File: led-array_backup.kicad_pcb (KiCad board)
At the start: 4 copper layers, 180.2 x 119.8 mm, 1226 parts, among them J1 Conn_01x04_Pin, J2 USB_B_Micro, Q1 Q_NMOS_GDS, Q2 Q_NMOS_GDS, Q3 Q_NMOS_GDS, Q4 Q_NMOS_GDS, Q5 Q_NMOS_GDS, Q6 Q_NMOS_GDS, Q7 Q_NMOS_GDS, Q8 Q_NMOS_GDS, U1 TPS54331DR, U10 74HC595, U11 74HC595, U12 74HC595, U13 74HC595, U14 74HC595, U15 74HC595, U16 74HC595, U17 74HC595, U18 74HC595, U2 STM32F103C8T6, U3 74HC595, U4 74HC595, U5 74HC595, U6 74HC595, U7 74HC595, U8 74HC595, U9 74HC595, Y1 16MHz

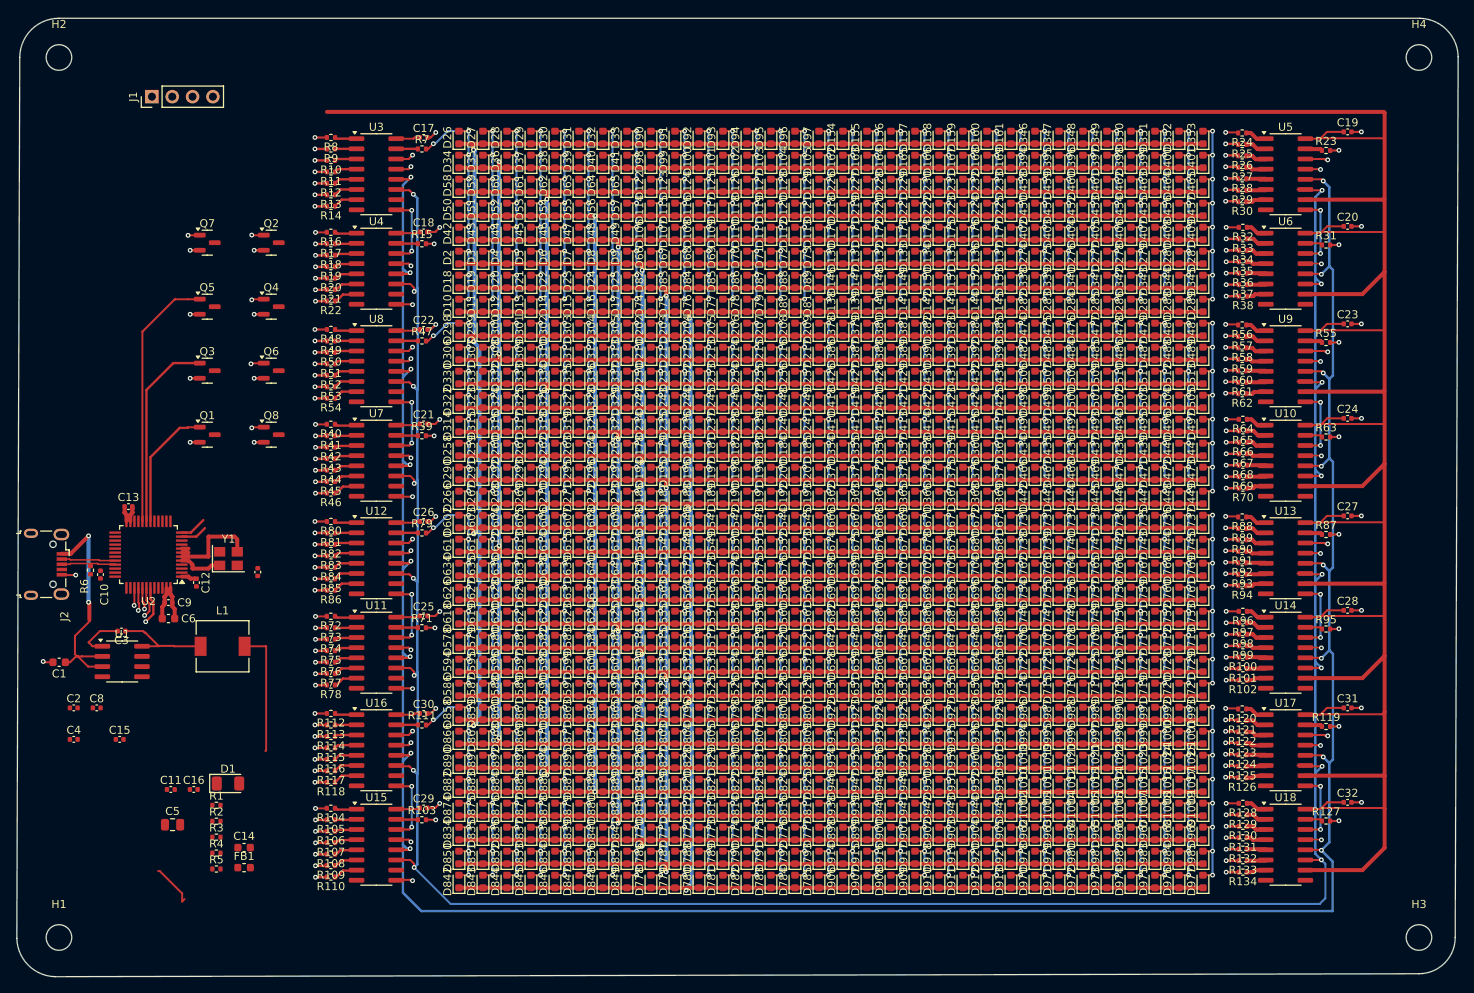
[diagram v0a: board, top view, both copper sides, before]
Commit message: Set up RCLK and SRCLK lines
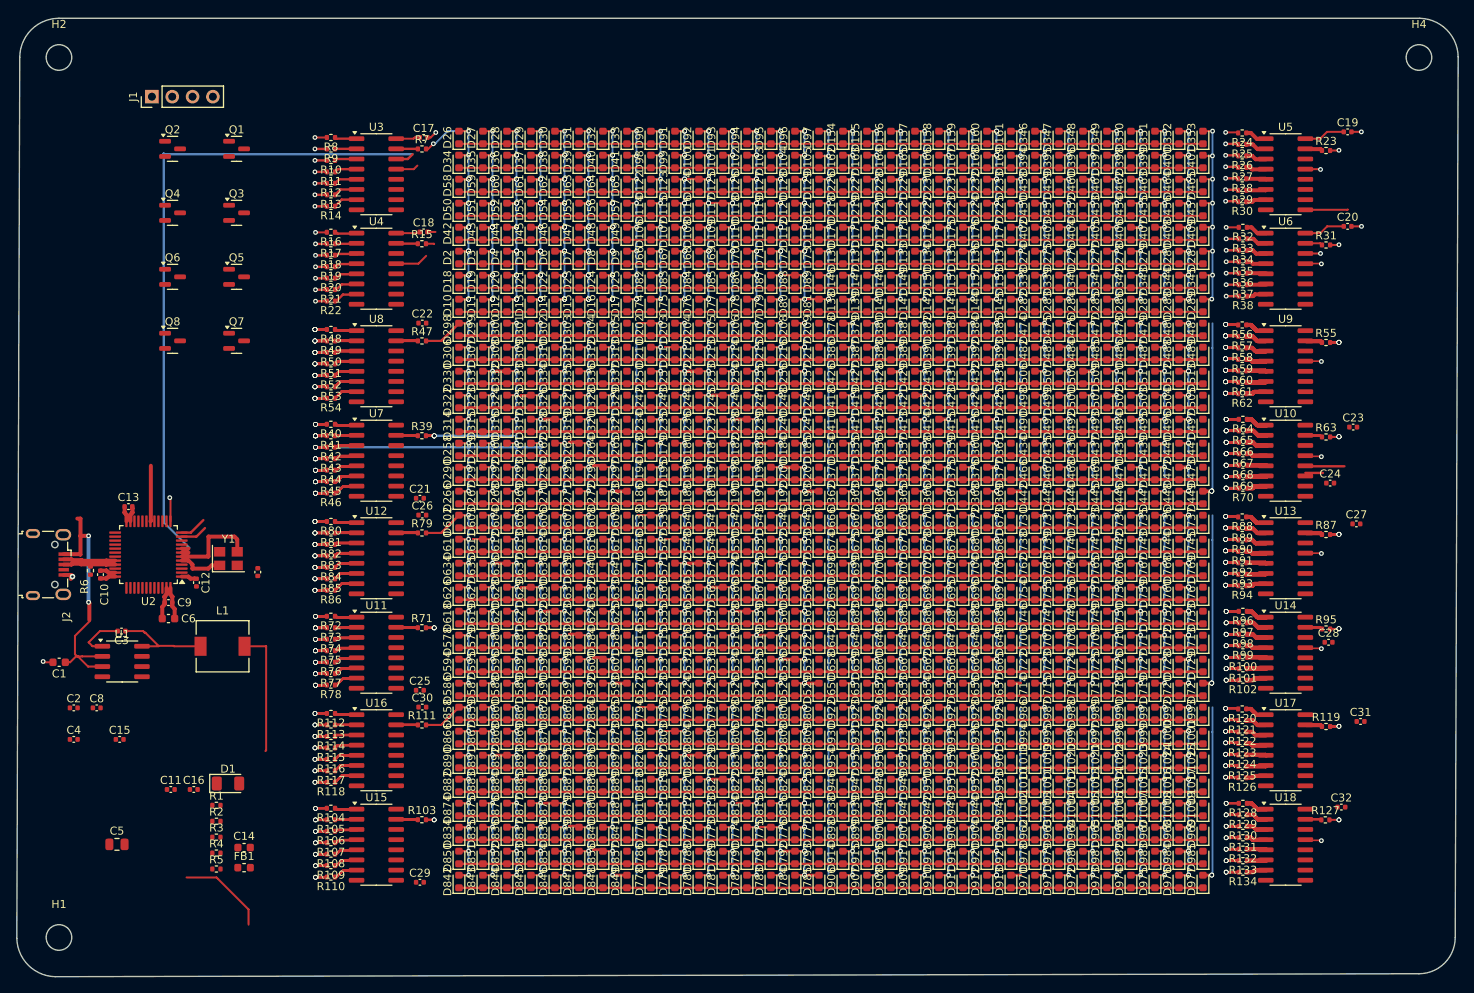
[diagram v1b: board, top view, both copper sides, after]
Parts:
- removed H3: MountingHole, MountingHole:MountingHole_3.2mm_M3
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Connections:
- D10 pad 1: /K7 -> /LED Group 0/Led Module 1/K7
- D100 pad 1: /K1 -> /LED Group 0/Led Module 1/K1
- D1000 pad 1: /K1 -> /LED Group 3/Led Module 1/K1
- D1001 pad 1: /K1 -> /LED Group 3/Led Module 1/K1
- D1002 pad 1: /K4 -> /LED Group 3/Led Module 1/K4
- D1003 pad 1: /K4 -> /LED Group 3/Led Module 1/K4
- D1004 pad 1: /K4 -> /LED Group 3/Led Module 1/K4
- D1005 pad 1: /K4 -> /LED Group 3/Led Module 1/K4
- D1006 pad 1: /K4 -> /LED Group 3/Led Module 1/K4
- D1007 pad 1: /K4 -> /LED Group 3/Led Module 1/K4
- D1008 pad 1: /K4 -> /LED Group 3/Led Module 1/K4
- D1009 pad 1: /K4 -> /LED Group 3/Led Module 1/K4
- D101 pad 1: /K1 -> /LED Group 0/Led Module 1/K1
- D1010 pad 1: /K3 -> /LED Group 3/Led Module 1/K3
- D1011 pad 1: /K3 -> /LED Group 3/Led Module 1/K3
- D1012 pad 1: /K3 -> /LED Group 3/Led Module 1/K3
- D1013 pad 1: /K3 -> /LED Group 3/Led Module 1/K3
- D1014 pad 1: /K3 -> /LED Group 3/Led Module 1/K3
- D1015 pad 1: /K3 -> /LED Group 3/Led Module 1/K3
- D1016 pad 1: /K3 -> /LED Group 3/Led Module 1/K3
- D1017 pad 1: /K3 -> /LED Group 3/Led Module 1/K3
- D1018 pad 1: /K2 -> /LED Group 3/Led Module 1/K2
- D1019 pad 1: /K2 -> /LED Group 3/Led Module 1/K2
- D102 pad 1: /K1 -> /LED Group 0/Led Module 1/K1
- D1020 pad 1: /K2 -> /LED Group 3/Led Module 1/K2
- D1021 pad 1: /K2 -> /LED Group 3/Led Module 1/K2
- D1022 pad 1: /K2 -> /LED Group 3/Led Module 1/K2
- D1023 pad 1: /K2 -> /LED Group 3/Led Module 1/K2
- D1024 pad 1: /K2 -> /LED Group 3/Led Module 1/K2
- D1025 pad 1: /K2 -> /LED Group 3/Led Module 1/K2
- D103 pad 1: /K1 -> /LED Group 0/Led Module 1/K1
- D104 pad 1: /K1 -> /LED Group 0/Led Module 1/K1
- D105 pad 1: /K1 -> /LED Group 0/Led Module 1/K1
- D106 pad 1: /K4 -> /LED Group 0/Led Module 1/K4
- D107 pad 1: /K4 -> /LED Group 0/Led Module 1/K4
- D108 pad 1: /K4 -> /LED Group 0/Led Module 1/K4
- D109 pad 1: /K4 -> /LED Group 0/Led Module 1/K4
- D11 pad 1: /K7 -> /LED Group 0/Led Module 1/K7
- D110 pad 1: /K4 -> /LED Group 0/Led Module 1/K4
- D111 pad 1: /K4 -> /LED Group 0/Led Module 1/K4
- D112 pad 1: /K4 -> /LED Group 0/Led Module 1/K4
- D113 pad 1: /K4 -> /LED Group 0/Led Module 1/K4
- D114 pad 1: /K3 -> /LED Group 0/Led Module 1/K3
- D115 pad 1: /K3 -> /LED Group 0/Led Module 1/K3
- D116 pad 1: /K3 -> /LED Group 0/Led Module 1/K3
- D117 pad 1: /K3 -> /LED Group 0/Led Module 1/K3
- D118 pad 1: /K3 -> /LED Group 0/Led Module 1/K3
- D119 pad 1: /K3 -> /LED Group 0/Led Module 1/K3
- D12 pad 1: /K7 -> /LED Group 0/Led Module 1/K7
- D120 pad 1: /K3 -> /LED Group 0/Led Module 1/K3
- D121 pad 1: /K3 -> /LED Group 0/Led Module 1/K3
- D122 pad 1: /K2 -> /LED Group 0/Led Module 1/K2
- D123 pad 1: /K2 -> /LED Group 0/Led Module 1/K2
- D124 pad 1: /K2 -> /LED Group 0/Led Module 1/K2
- D125 pad 1: /K2 -> /LED Group 0/Led Module 1/K2
- D126 pad 1: /K2 -> /LED Group 0/Led Module 1/K2
- D127 pad 1: /K2 -> /LED Group 0/Led Module 1/K2
- D128 pad 1: /K2 -> /LED Group 0/Led Module 1/K2
- D129 pad 1: /K2 -> /LED Group 0/Led Module 1/K2
- D13 pad 1: /K7 -> /LED Group 0/Led Module 1/K7
- D130 pad 1: /K5 -> /LED Group 0/Led Module 1/K5
- D131 pad 1: /K5 -> /LED Group 0/Led Module 1/K5
- D132 pad 1: /K5 -> /LED Group 0/Led Module 1/K5
- D133 pad 1: /K5 -> /LED Group 0/Led Module 1/K5
- D134 pad 1: /K5 -> /LED Group 0/Led Module 1/K5
- D135 pad 1: /K5 -> /LED Group 0/Led Module 1/K5
- D136 pad 1: /K5 -> /LED Group 0/Led Module 1/K5
- D137 pad 1: /K5 -> /LED Group 0/Led Module 1/K5
- D138 pad 1: /K7 -> /LED Group 0/Led Module 1/K7
- D139 pad 1: /K7 -> /LED Group 0/Led Module 1/K7
- D14 pad 1: /K7 -> /LED Group 0/Led Module 1/K7
- D140 pad 1: /K7 -> /LED Group 0/Led Module 1/K7
- D141 pad 1: /K7 -> /LED Group 0/Led Module 1/K7
- D142 pad 1: /K7 -> /LED Group 0/Led Module 1/K7
- D143 pad 1: /K7 -> /LED Group 0/Led Module 1/K7
- D144 pad 1: /K7 -> /LED Group 0/Led Module 1/K7
- D145 pad 1: /K7 -> /LED Group 0/Led Module 1/K7
- D146 pad 1: /K6 -> /LED Group 0/Led Module 1/K6
- D147 pad 1: /K6 -> /LED Group 0/Led Module 1/K6
- D148 pad 1: /K6 -> /LED Group 0/Led Module 1/K6
- D149 pad 1: /K6 -> /LED Group 0/Led Module 1/K6
- D15 pad 1: /K7 -> /LED Group 0/Led Module 1/K7
- D150 pad 1: /K6 -> /LED Group 0/Led Module 1/K6
- D151 pad 1: /K6 -> /LED Group 0/Led Module 1/K6
- D152 pad 1: /K6 -> /LED Group 0/Led Module 1/K6
- D153 pad 1: /K6 -> /LED Group 0/Led Module 1/K6
- D154 pad 1: /K0 -> /LED Group 0/Led Module 1/K0
- D155 pad 1: /K0 -> /LED Group 0/Led Module 1/K0
- D156 pad 1: /K0 -> /LED Group 0/Led Module 1/K0
- D157 pad 1: /K0 -> /LED Group 0/Led Module 1/K0
- D158 pad 1: /K0 -> /LED Group 0/Led Module 1/K0
- D159 pad 1: /K0 -> /LED Group 0/Led Module 1/K0
- D16 pad 1: /K7 -> /LED Group 0/Led Module 1/K7
- D160 pad 1: /K0 -> /LED Group 0/Led Module 1/K0
- D161 pad 1: /K0 -> /LED Group 0/Led Module 1/K0
- D162 pad 1: /K1 -> /LED Group 0/Led Module 1/K1
- D163 pad 1: /K1 -> /LED Group 0/Led Module 1/K1
- D164 pad 1: /K1 -> /LED Group 0/Led Module 1/K1
- D165 pad 1: /K1 -> /LED Group 0/Led Module 1/K1
- D166 pad 1: /K1 -> /LED Group 0/Led Module 1/K1
- D167 pad 1: /K1 -> /LED Group 0/Led Module 1/K1
- D168 pad 1: /K1 -> /LED Group 0/Led Module 1/K1
- D169 pad 1: /K1 -> /LED Group 0/Led Module 1/K1
- D17 pad 1: /K7 -> /LED Group 0/Led Module 1/K7
- D170 pad 1: /K4 -> /LED Group 0/Led Module 1/K4
- D171 pad 1: /K4 -> /LED Group 0/Led Module 1/K4
- D172 pad 1: /K4 -> /LED Group 0/Led Module 1/K4
- D173 pad 1: /K4 -> /LED Group 0/Led Module 1/K4
- D174 pad 1: /K4 -> /LED Group 0/Led Module 1/K4
- D175 pad 1: /K4 -> /LED Group 0/Led Module 1/K4
- D176 pad 1: /K4 -> /LED Group 0/Led Module 1/K4
- D177 pad 1: /K4 -> /LED Group 0/Led Module 1/K4
- D178 pad 1: /K5 -> /LED Group 1/Led Module 1/K5
- D179 pad 1: /K5 -> /LED Group 1/Led Module 1/K5
- D18 pad 1: /K6 -> /LED Group 0/Led Module 1/K6
- D180 pad 1: /K5 -> /LED Group 1/Led Module 1/K5
- D181 pad 1: /K5 -> /LED Group 1/Led Module 1/K5
- D182 pad 1: /K5 -> /LED Group 1/Led Module 1/K5
- D183 pad 1: /K5 -> /LED Group 1/Led Module 1/K5
- D184 pad 1: /K5 -> /LED Group 1/Led Module 1/K5
- D185 pad 1: /K5 -> /LED Group 1/Led Module 1/K5
- D186 pad 1: /K7 -> /LED Group 1/Led Module 1/K7
- D187 pad 1: /K7 -> /LED Group 1/Led Module 1/K7
- D188 pad 1: /K7 -> /LED Group 1/Led Module 1/K7
- D189 pad 1: /K7 -> /LED Group 1/Led Module 1/K7
- D19 pad 1: /K6 -> /LED Group 0/Led Module 1/K6
- D190 pad 1: /K7 -> /LED Group 1/Led Module 1/K7
- D191 pad 1: /K7 -> /LED Group 1/Led Module 1/K7
- D192 pad 1: /K7 -> /LED Group 1/Led Module 1/K7
- D193 pad 1: /K7 -> /LED Group 1/Led Module 1/K7
- D194 pad 1: /K6 -> /LED Group 1/Led Module 1/K6
- D195 pad 1: /K6 -> /LED Group 1/Led Module 1/K6
- D196 pad 1: /K6 -> /LED Group 1/Led Module 1/K6
- D197 pad 1: /K6 -> /LED Group 1/Led Module 1/K6
- D198 pad 1: /K6 -> /LED Group 1/Led Module 1/K6
- D199 pad 1: /K6 -> /LED Group 1/Led Module 1/K6
- D2 pad 1: /K5 -> /LED Group 0/Led Module 1/K5
- D20 pad 1: /K6 -> /LED Group 0/Led Module 1/K6
- D200 pad 1: /K6 -> /LED Group 1/Led Module 1/K6
- D201 pad 1: /K6 -> /LED Group 1/Led Module 1/K6
- D202 pad 1: /K0 -> /LED Group 1/Led Module 1/K0
- D203 pad 1: /K0 -> /LED Group 1/Led Module 1/K0
- D204 pad 1: /K0 -> /LED Group 1/Led Module 1/K0
- D205 pad 1: /K0 -> /LED Group 1/Led Module 1/K0
- D206 pad 1: /K0 -> /LED Group 1/Led Module 1/K0
- D207 pad 1: /K0 -> /LED Group 1/Led Module 1/K0
- D208 pad 1: /K0 -> /LED Group 1/Led Module 1/K0
- D209 pad 1: /K0 -> /LED Group 1/Led Module 1/K0
- D21 pad 1: /K6 -> /LED Group 0/Led Module 1/K6
- D210 pad 1: /K1 -> /LED Group 1/Led Module 1/K1
- D211 pad 1: /K1 -> /LED Group 1/Led Module 1/K1
- D212 pad 1: /K1 -> /LED Group 1/Led Module 1/K1
- D213 pad 1: /K1 -> /LED Group 1/Led Module 1/K1
- D214 pad 1: /K1 -> /LED Group 1/Led Module 1/K1
- D215 pad 1: /K1 -> /LED Group 1/Led Module 1/K1
- D216 pad 1: /K1 -> /LED Group 1/Led Module 1/K1
- D217 pad 1: /K1 -> /LED Group 1/Led Module 1/K1
- D218 pad 1: /K3 -> /LED Group 0/Led Module 1/K3
- D219 pad 1: /K3 -> /LED Group 0/Led Module 1/K3
- D22 pad 1: /K6 -> /LED Group 0/Led Module 1/K6
- D220 pad 1: /K3 -> /LED Group 0/Led Module 1/K3
- D221 pad 1: /K3 -> /LED Group 0/Led Module 1/K3
- D222 pad 1: /K3 -> /LED Group 0/Led Module 1/K3
- D223 pad 1: /K3 -> /LED Group 0/Led Module 1/K3
- D224 pad 1: /K3 -> /LED Group 0/Led Module 1/K3
- D225 pad 1: /K3 -> /LED Group 0/Led Module 1/K3
- D226 pad 1: /K2 -> /LED Group 0/Led Module 1/K2
- D227 pad 1: /K2 -> /LED Group 0/Led Module 1/K2
- D228 pad 1: /K2 -> /LED Group 0/Led Module 1/K2
- D229 pad 1: /K2 -> /LED Group 0/Led Module 1/K2
- D23 pad 1: /K6 -> /LED Group 0/Led Module 1/K6
- D230 pad 1: /K2 -> /LED Group 0/Led Module 1/K2
- D231 pad 1: /K2 -> /LED Group 0/Led Module 1/K2
- D232 pad 1: /K2 -> /LED Group 0/Led Module 1/K2
- D233 pad 1: /K2 -> /LED Group 0/Led Module 1/K2
- D234 pad 1: /K4 -> /LED Group 1/Led Module 1/K4
- D235 pad 1: /K4 -> /LED Group 1/Led Module 1/K4
- D236 pad 1: /K4 -> /LED Group 1/Led Module 1/K4
- D237 pad 1: /K4 -> /LED Group 1/Led Module 1/K4
- D238 pad 1: /K4 -> /LED Group 1/Led Module 1/K4
- D239 pad 1: /K4 -> /LED Group 1/Led Module 1/K4
- D24 pad 1: /K6 -> /LED Group 0/Led Module 1/K6
- D240 pad 1: /K4 -> /LED Group 1/Led Module 1/K4
- D241 pad 1: /K4 -> /LED Group 1/Led Module 1/K4
- D242 pad 1: /K3 -> /LED Group 1/Led Module 1/K3
- D243 pad 1: /K3 -> /LED Group 1/Led Module 1/K3
- D244 pad 1: /K3 -> /LED Group 1/Led Module 1/K3
- D245 pad 1: /K3 -> /LED Group 1/Led Module 1/K3
- D246 pad 1: /K3 -> /LED Group 1/Led Module 1/K3
- D247 pad 1: /K3 -> /LED Group 1/Led Module 1/K3
- D248 pad 1: /K3 -> /LED Group 1/Led Module 1/K3
- D249 pad 1: /K3 -> /LED Group 1/Led Module 1/K3
- D25 pad 1: /K6 -> /LED Group 0/Led Module 1/K6
- D250 pad 1: /K2 -> /LED Group 1/Led Module 1/K2
- D251 pad 1: /K2 -> /LED Group 1/Led Module 1/K2
- D252 pad 1: /K2 -> /LED Group 1/Led Module 1/K2
- D253 pad 1: /K2 -> /LED Group 1/Led Module 1/K2
- D254 pad 1: /K2 -> /LED Group 1/Led Module 1/K2
- D255 pad 1: /K2 -> /LED Group 1/Led Module 1/K2
- D256 pad 1: /K2 -> /LED Group 1/Led Module 1/K2
- D257 pad 1: /K2 -> /LED Group 1/Led Module 1/K2
- D258 pad 1: /K5 -> /LED Group 1/Led Module 1/K5
- D259 pad 1: /K5 -> /LED Group 1/Led Module 1/K5
- D26 pad 1: /K0 -> /LED Group 0/Led Module 1/K0
- D260 pad 1: /K5 -> /LED Group 1/Led Module 1/K5
- D261 pad 1: /K5 -> /LED Group 1/Led Module 1/K5
- D262 pad 1: /K5 -> /LED Group 1/Led Module 1/K5
- D263 pad 1: /K5 -> /LED Group 1/Led Module 1/K5
- D264 pad 1: /K5 -> /LED Group 1/Led Module 1/K5
- D265 pad 1: /K5 -> /LED Group 1/Led Module 1/K5
- D266 pad 1: /K7 -> /LED Group 1/Led Module 1/K7
- D267 pad 1: /K7 -> /LED Group 1/Led Module 1/K7
- D268 pad 1: /K7 -> /LED Group 1/Led Module 1/K7
- D269 pad 1: /K7 -> /LED Group 1/Led Module 1/K7
- D27 pad 1: /K0 -> /LED Group 0/Led Module 1/K0
- D270 pad 1: /K7 -> /LED Group 1/Led Module 1/K7
- D271 pad 1: /K7 -> /LED Group 1/Led Module 1/K7
- D272 pad 1: /K7 -> /LED Group 1/Led Module 1/K7
- D273 pad 1: /K7 -> /LED Group 1/Led Module 1/K7
- D274 pad 1: /K5 -> /LED Group 0/Led Module 1/K5
- D275 pad 1: /K5 -> /LED Group 0/Led Module 1/K5
- D276 pad 1: /K5 -> /LED Group 0/Led Module 1/K5
- D277 pad 1: /K5 -> /LED Group 0/Led Module 1/K5
- D278 pad 1: /K5 -> /LED Group 0/Led Module 1/K5
- D279 pad 1: /K5 -> /LED Group 0/Led Module 1/K5
- D28 pad 1: /K0 -> /LED Group 0/Led Module 1/K0
- D280 pad 1: /K5 -> /LED Group 0/Led Module 1/K5
- D281 pad 1: /K5 -> /LED Group 0/Led Module 1/K5
- D282 pad 1: /K7 -> /LED Group 0/Led Module 1/K7
- D283 pad 1: /K7 -> /LED Group 0/Led Module 1/K7
- D284 pad 1: /K7 -> /LED Group 0/Led Module 1/K7
- D285 pad 1: /K7 -> /LED Group 0/Led Module 1/K7
- D286 pad 1: /K7 -> /LED Group 0/Led Module 1/K7
- D287 pad 1: /K7 -> /LED Group 0/Led Module 1/K7
- D288 pad 1: /K7 -> /LED Group 0/Led Module 1/K7
- D289 pad 1: /K7 -> /LED Group 0/Led Module 1/K7
- D29 pad 1: /K0 -> /LED Group 0/Led Module 1/K0
- D290 pad 1: /K6 -> /LED Group 1/Led Module 1/K6
- D291 pad 1: /K6 -> /LED Group 1/Led Module 1/K6
- D292 pad 1: /K6 -> /LED Group 1/Led Module 1/K6
- D293 pad 1: /K6 -> /LED Group 1/Led Module 1/K6
- D294 pad 1: /K6 -> /LED Group 1/Led Module 1/K6
- D295 pad 1: /K6 -> /LED Group 1/Led Module 1/K6
- D296 pad 1: /K6 -> /LED Group 1/Led Module 1/K6
- D297 pad 1: /K6 -> /LED Group 1/Led Module 1/K6
- D298 pad 1: /K0 -> /LED Group 1/Led Module 1/K0
- D299 pad 1: /K0 -> /LED Group 1/Led Module 1/K0
- D3 pad 1: /K5 -> /LED Group 0/Led Module 1/K5
- D30 pad 1: /K0 -> /LED Group 0/Led Module 1/K0
- D300 pad 1: /K0 -> /LED Group 1/Led Module 1/K0
- D301 pad 1: /K0 -> /LED Group 1/Led Module 1/K0
- D302 pad 1: /K0 -> /LED Group 1/Led Module 1/K0
- D303 pad 1: /K0 -> /LED Group 1/Led Module 1/K0
- D304 pad 1: /K0 -> /LED Group 1/Led Module 1/K0
- D305 pad 1: /K0 -> /LED Group 1/Led Module 1/K0
- D306 pad 1: /K1 -> /LED Group 1/Led Module 1/K1
- D307 pad 1: /K1 -> /LED Group 1/Led Module 1/K1
- D308 pad 1: /K1 -> /LED Group 1/Led Module 1/K1
- D309 pad 1: /K1 -> /LED Group 1/Led Module 1/K1
- D31 pad 1: /K0 -> /LED Group 0/Led Module 1/K0
- D310 pad 1: /K1 -> /LED Group 1/Led Module 1/K1
- D311 pad 1: /K1 -> /LED Group 1/Led Module 1/K1
- D312 pad 1: /K1 -> /LED Group 1/Led Module 1/K1
- D313 pad 1: /K1 -> /LED Group 1/Led Module 1/K1
- D314 pad 1: /K4 -> /LED Group 1/Led Module 1/K4
- D315 pad 1: /K4 -> /LED Group 1/Led Module 1/K4
- D316 pad 1: /K4 -> /LED Group 1/Led Module 1/K4
- D317 pad 1: /K4 -> /LED Group 1/Led Module 1/K4
- D318 pad 1: /K4 -> /LED Group 1/Led Module 1/K4
- D319 pad 1: /K4 -> /LED Group 1/Led Module 1/K4
- D32 pad 1: /K0 -> /LED Group 0/Led Module 1/K0
- D320 pad 1: /K4 -> /LED Group 1/Led Module 1/K4
- D321 pad 1: /K4 -> /LED Group 1/Led Module 1/K4
- D322 pad 1: /K3 -> /LED Group 1/Led Module 1/K3
- D323 pad 1: /K3 -> /LED Group 1/Led Module 1/K3
- D324 pad 1: /K3 -> /LED Group 1/Led Module 1/K3
- D325 pad 1: /K3 -> /LED Group 1/Led Module 1/K3
- D326 pad 1: /K3 -> /LED Group 1/Led Module 1/K3
- D327 pad 1: /K3 -> /LED Group 1/Led Module 1/K3
- D328 pad 1: /K3 -> /LED Group 1/Led Module 1/K3
- D329 pad 1: /K3 -> /LED Group 1/Led Module 1/K3
- D33 pad 1: /K0 -> /LED Group 0/Led Module 1/K0
- D330 pad 1: /K2 -> /LED Group 1/Led Module 1/K2
- D331 pad 1: /K2 -> /LED Group 1/Led Module 1/K2
- D332 pad 1: /K2 -> /LED Group 1/Led Module 1/K2
- D333 pad 1: /K2 -> /LED Group 1/Led Module 1/K2
- D334 pad 1: /K2 -> /LED Group 1/Led Module 1/K2
- D335 pad 1: /K2 -> /LED Group 1/Led Module 1/K2
- D336 pad 1: /K2 -> /LED Group 1/Led Module 1/K2
- D337 pad 1: /K2 -> /LED Group 1/Led Module 1/K2
- D338 pad 1: /K6 -> /LED Group 0/Led Module 1/K6
- D339 pad 1: /K6 -> /LED Group 0/Led Module 1/K6
- D34 pad 1: /K1 -> /LED Group 0/Led Module 1/K1
- D340 pad 1: /K6 -> /LED Group 0/Led Module 1/K6
- D341 pad 1: /K6 -> /LED Group 0/Led Module 1/K6
- D342 pad 1: /K6 -> /LED Group 0/Led Module 1/K6
- D343 pad 1: /K6 -> /LED Group 0/Led Module 1/K6
- D344 pad 1: /K6 -> /LED Group 0/Led Module 1/K6
- D345 pad 1: /K6 -> /LED Group 0/Led Module 1/K6
- D346 pad 1: /K0 -> /LED Group 0/Led Module 1/K0
- D347 pad 1: /K0 -> /LED Group 0/Led Module 1/K0
- D348 pad 1: /K0 -> /LED Group 0/Led Module 1/K0
- D349 pad 1: /K0 -> /LED Group 0/Led Module 1/K0
- D35 pad 1: /K1 -> /LED Group 0/Led Module 1/K1
- D350 pad 1: /K0 -> /LED Group 0/Led Module 1/K0
- D351 pad 1: /K0 -> /LED Group 0/Led Module 1/K0
- D352 pad 1: /K0 -> /LED Group 0/Led Module 1/K0
- D353 pad 1: /K0 -> /LED Group 0/Led Module 1/K0
- D354 pad 1: /K5 -> /LED Group 1/Led Module 1/K5
- D355 pad 1: /K5 -> /LED Group 1/Led Module 1/K5
- D356 pad 1: /K5 -> /LED Group 1/Led Module 1/K5
- D357 pad 1: /K5 -> /LED Group 1/Led Module 1/K5
- D358 pad 1: /K5 -> /LED Group 1/Led Module 1/K5
- D359 pad 1: /K5 -> /LED Group 1/Led Module 1/K5
- D36 pad 1: /K1 -> /LED Group 0/Led Module 1/K1
- D360 pad 1: /K5 -> /LED Group 1/Led Module 1/K5
- D361 pad 1: /K5 -> /LED Group 1/Led Module 1/K5
- D362 pad 1: /K7 -> /LED Group 1/Led Module 1/K7
- D363 pad 1: /K7 -> /LED Group 1/Led Module 1/K7
- D364 pad 1: /K7 -> /LED Group 1/Led Module 1/K7
- D365 pad 1: /K7 -> /LED Group 1/Led Module 1/K7
- D366 pad 1: /K7 -> /LED Group 1/Led Module 1/K7
- D367 pad 1: /K7 -> /LED Group 1/Led Module 1/K7
- D368 pad 1: /K7 -> /LED Group 1/Led Module 1/K7
- D369 pad 1: /K7 -> /LED Group 1/Led Module 1/K7
- D37 pad 1: /K1 -> /LED Group 0/Led Module 1/K1
- D370 pad 1: /K6 -> /LED Group 1/Led Module 1/K6
- D371 pad 1: /K6 -> /LED Group 1/Led Module 1/K6
- D372 pad 1: /K6 -> /LED Group 1/Led Module 1/K6
- D373 pad 1: /K6 -> /LED Group 1/Led Module 1/K6
- D374 pad 1: /K6 -> /LED Group 1/Led Module 1/K6
- D375 pad 1: /K6 -> /LED Group 1/Led Module 1/K6
- D376 pad 1: /K6 -> /LED Group 1/Led Module 1/K6
- D377 pad 1: /K6 -> /LED Group 1/Led Module 1/K6
- D378 pad 1: /K0 -> /LED Group 1/Led Module 1/K0
- D379 pad 1: /K0 -> /LED Group 1/Led Module 1/K0
- D38 pad 1: /K1 -> /LED Group 0/Led Module 1/K1
- D380 pad 1: /K0 -> /LED Group 1/Led Module 1/K0
- D381 pad 1: /K0 -> /LED Group 1/Led Module 1/K0
- D382 pad 1: /K0 -> /LED Group 1/Led Module 1/K0
- D383 pad 1: /K0 -> /LED Group 1/Led Module 1/K0
- D384 pad 1: /K0 -> /LED Group 1/Led Module 1/K0
- D385 pad 1: /K0 -> /LED Group 1/Led Module 1/K0
- D386 pad 1: /K1 -> /LED Group 1/Led Module 1/K1
- D387 pad 1: /K1 -> /LED Group 1/Led Module 1/K1
- D388 pad 1: /K1 -> /LED Group 1/Led Module 1/K1
- D389 pad 1: /K1 -> /LED Group 1/Led Module 1/K1
- D39 pad 1: /K1 -> /LED Group 0/Led Module 1/K1
- D390 pad 1: /K1 -> /LED Group 1/Led Module 1/K1
- D391 pad 1: /K1 -> /LED Group 1/Led Module 1/K1
- D392 pad 1: /K1 -> /LED Group 1/Led Module 1/K1
- D393 pad 1: /K1 -> /LED Group 1/Led Module 1/K1
- D394 pad 1: /K1 -> /LED Group 0/Led Module 1/K1
- D395 pad 1: /K1 -> /LED Group 0/Led Module 1/K1
- D396 pad 1: /K1 -> /LED Group 0/Led Module 1/K1
- D397 pad 1: /K1 -> /LED Group 0/Led Module 1/K1
- D398 pad 1: /K1 -> /LED Group 0/Led Module 1/K1
- D399 pad 1: /K1 -> /LED Group 0/Led Module 1/K1
- D4 pad 1: /K5 -> /LED Group 0/Led Module 1/K5
- D40 pad 1: /K1 -> /LED Group 0/Led Module 1/K1
- D400 pad 1: /K1 -> /LED Group 0/Led Module 1/K1
- D401 pad 1: /K1 -> /LED Group 0/Led Module 1/K1
- D402 pad 1: /K4 -> /LED Group 0/Led Module 1/K4
- D403 pad 1: /K4 -> /LED Group 0/Led Module 1/K4
- D404 pad 1: /K4 -> /LED Group 0/Led Module 1/K4
- D405 pad 1: /K4 -> /LED Group 0/Led Module 1/K4
- D406 pad 1: /K4 -> /LED Group 0/Led Module 1/K4
- D407 pad 1: /K4 -> /LED Group 0/Led Module 1/K4
- D408 pad 1: /K4 -> /LED Group 0/Led Module 1/K4
- D409 pad 1: /K4 -> /LED Group 0/Led Module 1/K4
- D41 pad 1: /K1 -> /LED Group 0/Led Module 1/K1
- D410 pad 1: /K4 -> /LED Group 1/Led Module 1/K4
- D411 pad 1: /K4 -> /LED Group 1/Led Module 1/K4
- D412 pad 1: /K4 -> /LED Group 1/Led Module 1/K4
- D413 pad 1: /K4 -> /LED Group 1/Led Module 1/K4
- D414 pad 1: /K4 -> /LED Group 1/Led Module 1/K4
- D415 pad 1: /K4 -> /LED Group 1/Led Module 1/K4
- D416 pad 1: /K4 -> /LED Group 1/Led Module 1/K4
- D417 pad 1: /K4 -> /LED Group 1/Led Module 1/K4
- D418 pad 1: /K3 -> /LED Group 1/Led Module 1/K3
- D419 pad 1: /K3 -> /LED Group 1/Led Module 1/K3
- D42 pad 1: /K4 -> /LED Group 0/Led Module 1/K4
- D420 pad 1: /K3 -> /LED Group 1/Led Module 1/K3
- D421 pad 1: /K3 -> /LED Group 1/Led Module 1/K3
- D422 pad 1: /K3 -> /LED Group 1/Led Module 1/K3
- D423 pad 1: /K3 -> /LED Group 1/Led Module 1/K3
- D424 pad 1: /K3 -> /LED Group 1/Led Module 1/K3
- D425 pad 1: /K3 -> /LED Group 1/Led Module 1/K3
- D426 pad 1: /K2 -> /LED Group 1/Led Module 1/K2
- D427 pad 1: /K2 -> /LED Group 1/Led Module 1/K2
- D428 pad 1: /K2 -> /LED Group 1/Led Module 1/K2
- D429 pad 1: /K2 -> /LED Group 1/Led Module 1/K2
- D43 pad 1: /K4 -> /LED Group 0/Led Module 1/K4
- D430 pad 1: /K2 -> /LED Group 1/Led Module 1/K2
- D431 pad 1: /K2 -> /LED Group 1/Led Module 1/K2
- D432 pad 1: /K2 -> /LED Group 1/Led Module 1/K2
- D433 pad 1: /K2 -> /LED Group 1/Led Module 1/K2
- D434 pad 1: /K5 -> /LED Group 1/Led Module 1/K5
- D435 pad 1: /K5 -> /LED Group 1/Led Module 1/K5
- D436 pad 1: /K5 -> /LED Group 1/Led Module 1/K5
- D437 pad 1: /K5 -> /LED Group 1/Led Module 1/K5
- D438 pad 1: /K5 -> /LED Group 1/Led Module 1/K5
- D439 pad 1: /K5 -> /LED Group 1/Led Module 1/K5
- D44 pad 1: /K4 -> /LED Group 0/Led Module 1/K4
- D440 pad 1: /K5 -> /LED Group 1/Led Module 1/K5
- D441 pad 1: /K5 -> /LED Group 1/Led Module 1/K5
- D442 pad 1: /K7 -> /LED Group 1/Led Module 1/K7
- D443 pad 1: /K7 -> /LED Group 1/Led Module 1/K7
- D444 pad 1: /K7 -> /LED Group 1/Led Module 1/K7
- D445 pad 1: /K7 -> /LED Group 1/Led Module 1/K7
- D446 pad 1: /K7 -> /LED Group 1/Led Module 1/K7
- D447 pad 1: /K7 -> /LED Group 1/Led Module 1/K7
- D448 pad 1: /K7 -> /LED Group 1/Led Module 1/K7
- D449 pad 1: /K7 -> /LED Group 1/Led Module 1/K7
- D45 pad 1: /K4 -> /LED Group 0/Led Module 1/K4
- D450 pad 1: /K3 -> /LED Group 0/Led Module 1/K3
- D451 pad 1: /K3 -> /LED Group 0/Led Module 1/K3
- D452 pad 1: /K3 -> /LED Group 0/Led Module 1/K3
- D453 pad 1: /K3 -> /LED Group 0/Led Module 1/K3
- D454 pad 1: /K3 -> /LED Group 0/Led Module 1/K3
- D455 pad 1: /K3 -> /LED Group 0/Led Module 1/K3
- D456 pad 1: /K3 -> /LED Group 0/Led Module 1/K3
- D457 pad 1: /K3 -> /LED Group 0/Led Module 1/K3
- D458 pad 1: /K2 -> /LED Group 0/Led Module 1/K2
- D459 pad 1: /K2 -> /LED Group 0/Led Module 1/K2
- D46 pad 1: /K4 -> /LED Group 0/Led Module 1/K4
- D460 pad 1: /K2 -> /LED Group 0/Led Module 1/K2
- D461 pad 1: /K2 -> /LED Group 0/Led Module 1/K2
- D462 pad 1: /K2 -> /LED Group 0/Led Module 1/K2
- D463 pad 1: /K2 -> /LED Group 0/Led Module 1/K2
- D464 pad 1: /K2 -> /LED Group 0/Led Module 1/K2
- D465 pad 1: /K2 -> /LED Group 0/Led Module 1/K2
- D466 pad 1: /K6 -> /LED Group 1/Led Module 1/K6
- D467 pad 1: /K6 -> /LED Group 1/Led Module 1/K6
- D468 pad 1: /K6 -> /LED Group 1/Led Module 1/K6
- D469 pad 1: /K6 -> /LED Group 1/Led Module 1/K6
- D47 pad 1: /K4 -> /LED Group 0/Led Module 1/K4
- D470 pad 1: /K6 -> /LED Group 1/Led Module 1/K6
- D471 pad 1: /K6 -> /LED Group 1/Led Module 1/K6
- D472 pad 1: /K6 -> /LED Group 1/Led Module 1/K6
- D473 pad 1: /K6 -> /LED Group 1/Led Module 1/K6
- D474 pad 1: /K0 -> /LED Group 1/Led Module 1/K0
- D475 pad 1: /K0 -> /LED Group 1/Led Module 1/K0
- D476 pad 1: /K0 -> /LED Group 1/Led Module 1/K0
- D477 pad 1: /K0 -> /LED Group 1/Led Module 1/K0
- D478 pad 1: /K0 -> /LED Group 1/Led Module 1/K0
- D479 pad 1: /K0 -> /LED Group 1/Led Module 1/K0
- D48 pad 1: /K4 -> /LED Group 0/Led Module 1/K4
- D480 pad 1: /K0 -> /LED Group 1/Led Module 1/K0
- D481 pad 1: /K0 -> /LED Group 1/Led Module 1/K0
- D482 pad 1: /K1 -> /LED Group 1/Led Module 1/K1
- D483 pad 1: /K1 -> /LED Group 1/Led Module 1/K1
- D484 pad 1: /K1 -> /LED Group 1/Led Module 1/K1
- D485 pad 1: /K1 -> /LED Group 1/Led Module 1/K1
- D486 pad 1: /K1 -> /LED Group 1/Led Module 1/K1
- D487 pad 1: /K1 -> /LED Group 1/Led Module 1/K1
- D488 pad 1: /K1 -> /LED Group 1/Led Module 1/K1
- D489 pad 1: /K1 -> /LED Group 1/Led Module 1/K1
- D49 pad 1: /K4 -> /LED Group 0/Led Module 1/K4
- D490 pad 1: /K4 -> /LED Group 1/Led Module 1/K4
- D491 pad 1: /K4 -> /LED Group 1/Led Module 1/K4
- D492 pad 1: /K4 -> /LED Group 1/Led Module 1/K4
- D493 pad 1: /K4 -> /LED Group 1/Led Module 1/K4
- D494 pad 1: /K4 -> /LED Group 1/Led Module 1/K4
- D495 pad 1: /K4 -> /LED Group 1/Led Module 1/K4
- D496 pad 1: /K4 -> /LED Group 1/Led Module 1/K4
- D497 pad 1: /K4 -> /LED Group 1/Led Module 1/K4
- D498 pad 1: /K3 -> /LED Group 1/Led Module 1/K3
- D499 pad 1: /K3 -> /LED Group 1/Led Module 1/K3
- D5 pad 1: /K5 -> /LED Group 0/Led Module 1/K5
- D50 pad 1: /K3 -> /LED Group 0/Led Module 1/K3
- D500 pad 1: /K3 -> /LED Group 1/Led Module 1/K3
- D501 pad 1: /K3 -> /LED Group 1/Led Module 1/K3
- D502 pad 1: /K3 -> /LED Group 1/Led Module 1/K3
- D503 pad 1: /K3 -> /LED Group 1/Led Module 1/K3
- D504 pad 1: /K3 -> /LED Group 1/Led Module 1/K3
- D505 pad 1: /K3 -> /LED Group 1/Led Module 1/K3
- D506 pad 1: /K2 -> /LED Group 1/Led Module 1/K2
- D507 pad 1: /K2 -> /LED Group 1/Led Module 1/K2
- D508 pad 1: /K2 -> /LED Group 1/Led Module 1/K2
- D509 pad 1: /K2 -> /LED Group 1/Led Module 1/K2
- D51 pad 1: /K3 -> /LED Group 0/Led Module 1/K3
- D510 pad 1: /K2 -> /LED Group 1/Led Module 1/K2
- D511 pad 1: /K2 -> /LED Group 1/Led Module 1/K2
- D512 pad 1: /K2 -> /LED Group 1/Led Module 1/K2
- D513 pad 1: /K2 -> /LED Group 1/Led Module 1/K2
- D514 pad 1: /K5 -> /LED Group 2/Led Module 1/K5
- D515 pad 1: /K5 -> /LED Group 2/Led Module 1/K5
- D516 pad 1: /K5 -> /LED Group 2/Led Module 1/K5
- D517 pad 1: /K5 -> /LED Group 2/Led Module 1/K5
- D518 pad 1: /K5 -> /LED Group 2/Led Module 1/K5
- D519 pad 1: /K5 -> /LED Group 2/Led Module 1/K5
- D52 pad 1: /K3 -> /LED Group 0/Led Module 1/K3
- D520 pad 1: /K5 -> /LED Group 2/Led Module 1/K5
- D521 pad 1: /K5 -> /LED Group 2/Led Module 1/K5
- D522 pad 1: /K7 -> /LED Group 2/Led Module 1/K7
- D523 pad 1: /K7 -> /LED Group 2/Led Module 1/K7
- D524 pad 1: /K7 -> /LED Group 2/Led Module 1/K7
- D525 pad 1: /K7 -> /LED Group 2/Led Module 1/K7
- D526 pad 1: /K7 -> /LED Group 2/Led Module 1/K7
- D527 pad 1: /K7 -> /LED Group 2/Led Module 1/K7
- D528 pad 1: /K7 -> /LED Group 2/Led Module 1/K7
- D529 pad 1: /K7 -> /LED Group 2/Led Module 1/K7
- D53 pad 1: /K3 -> /LED Group 0/Led Module 1/K3
- D530 pad 1: /K6 -> /LED Group 2/Led Module 1/K6
- D531 pad 1: /K6 -> /LED Group 2/Led Module 1/K6
- D532 pad 1: /K6 -> /LED Group 2/Led Module 1/K6
- D533 pad 1: /K6 -> /LED Group 2/Led Module 1/K6
- D534 pad 1: /K6 -> /LED Group 2/Led Module 1/K6
- D535 pad 1: /K6 -> /LED Group 2/Led Module 1/K6
- D536 pad 1: /K6 -> /LED Group 2/Led Module 1/K6
- D537 pad 1: /K6 -> /LED Group 2/Led Module 1/K6
- D538 pad 1: /K0 -> /LED Group 2/Led Module 1/K0
- D539 pad 1: /K0 -> /LED Group 2/Led Module 1/K0
- D54 pad 1: /K3 -> /LED Group 0/Led Module 1/K3
- D540 pad 1: /K0 -> /LED Group 2/Led Module 1/K0
- D541 pad 1: /K0 -> /LED Group 2/Led Module 1/K0
- D542 pad 1: /K0 -> /LED Group 2/Led Module 1/K0
- D543 pad 1: /K0 -> /LED Group 2/Led Module 1/K0
- D544 pad 1: /K0 -> /LED Group 2/Led Module 1/K0
- D545 pad 1: /K0 -> /LED Group 2/Led Module 1/K0
- D546 pad 1: /K1 -> /LED Group 2/Led Module 1/K1
- D547 pad 1: /K1 -> /LED Group 2/Led Module 1/K1
- D548 pad 1: /K1 -> /LED Group 2/Led Module 1/K1
- D549 pad 1: /K1 -> /LED Group 2/Led Module 1/K1
- D55 pad 1: /K3 -> /LED Group 0/Led Module 1/K3
- D550 pad 1: /K1 -> /LED Group 2/Led Module 1/K1
- D551 pad 1: /K1 -> /LED Group 2/Led Module 1/K1
- D552 pad 1: /K1 -> /LED Group 2/Led Module 1/K1
- D553 pad 1: /K1 -> /LED Group 2/Led Module 1/K1
- D554 pad 1: /K4 -> /LED Group 2/Led Module 1/K4
- D555 pad 1: /K4 -> /LED Group 2/Led Module 1/K4
- D556 pad 1: /K4 -> /LED Group 2/Led Module 1/K4
- D557 pad 1: /K4 -> /LED Group 2/Led Module 1/K4
- D558 pad 1: /K4 -> /LED Group 2/Led Module 1/K4
- D559 pad 1: /K4 -> /LED Group 2/Led Module 1/K4
- D56 pad 1: /K3 -> /LED Group 0/Led Module 1/K3
- D560 pad 1: /K4 -> /LED Group 2/Led Module 1/K4
- D561 pad 1: /K4 -> /LED Group 2/Led Module 1/K4
- D562 pad 1: /K3 -> /LED Group 2/Led Module 1/K3
- D563 pad 1: /K3 -> /LED Group 2/Led Module 1/K3
- D564 pad 1: /K3 -> /LED Group 2/Led Module 1/K3
- D565 pad 1: /K3 -> /LED Group 2/Led Module 1/K3
- D566 pad 1: /K3 -> /LED Group 2/Led Module 1/K3
- D567 pad 1: /K3 -> /LED Group 2/Led Module 1/K3
- D568 pad 1: /K3 -> /LED Group 2/Led Module 1/K3
- D569 pad 1: /K3 -> /LED Group 2/Led Module 1/K3
- D57 pad 1: /K3 -> /LED Group 0/Led Module 1/K3
- D570 pad 1: /K2 -> /LED Group 2/Led Module 1/K2
- D571 pad 1: /K2 -> /LED Group 2/Led Module 1/K2
- D572 pad 1: /K2 -> /LED Group 2/Led Module 1/K2
- D573 pad 1: /K2 -> /LED Group 2/Led Module 1/K2
- D574 pad 1: /K2 -> /LED Group 2/Led Module 1/K2
- D575 pad 1: /K2 -> /LED Group 2/Led Module 1/K2
- D576 pad 1: /K2 -> /LED Group 2/Led Module 1/K2
- D577 pad 1: /K2 -> /LED Group 2/Led Module 1/K2
- D578 pad 1: /K5 -> /LED Group 2/Led Module 1/K5
- D579 pad 1: /K5 -> /LED Group 2/Led Module 1/K5
- D58 pad 1: /K2 -> /LED Group 0/Led Module 1/K2
- D580 pad 1: /K5 -> /LED Group 2/Led Module 1/K5
- D581 pad 1: /K5 -> /LED Group 2/Led Module 1/K5
- D582 pad 1: /K5 -> /LED Group 2/Led Module 1/K5
- D583 pad 1: /K5 -> /LED Group 2/Led Module 1/K5
- D584 pad 1: /K5 -> /LED Group 2/Led Module 1/K5
- D585 pad 1: /K5 -> /LED Group 2/Led Module 1/K5
- D586 pad 1: /K7 -> /LED Group 2/Led Module 1/K7
- D587 pad 1: /K7 -> /LED Group 2/Led Module 1/K7
- D588 pad 1: /K7 -> /LED Group 2/Led Module 1/K7
- D589 pad 1: /K7 -> /LED Group 2/Led Module 1/K7
- D59 pad 1: /K2 -> /LED Group 0/Led Module 1/K2
- D590 pad 1: /K7 -> /LED Group 2/Led Module 1/K7
- D591 pad 1: /K7 -> /LED Group 2/Led Module 1/K7
- D592 pad 1: /K7 -> /LED Group 2/Led Module 1/K7
- D593 pad 1: /K7 -> /LED Group 2/Led Module 1/K7
- D594 pad 1: /K6 -> /LED Group 2/Led Module 1/K6
- D595 pad 1: /K6 -> /LED Group 2/Led Module 1/K6
- D596 pad 1: /K6 -> /LED Group 2/Led Module 1/K6
- D597 pad 1: /K6 -> /LED Group 2/Led Module 1/K6
- D598 pad 1: /K6 -> /LED Group 2/Led Module 1/K6
- D599 pad 1: /K6 -> /LED Group 2/Led Module 1/K6
- D6 pad 1: /K5 -> /LED Group 0/Led Module 1/K5
- D60 pad 1: /K2 -> /LED Group 0/Led Module 1/K2
- D600 pad 1: /K6 -> /LED Group 2/Led Module 1/K6
- D601 pad 1: /K6 -> /LED Group 2/Led Module 1/K6
- D602 pad 1: /K0 -> /LED Group 2/Led Module 1/K0
- D603 pad 1: /K0 -> /LED Group 2/Led Module 1/K0
- D604 pad 1: /K0 -> /LED Group 2/Led Module 1/K0
- D605 pad 1: /K0 -> /LED Group 2/Led Module 1/K0
- D606 pad 1: /K0 -> /LED Group 2/Led Module 1/K0
- D607 pad 1: /K0 -> /LED Group 2/Led Module 1/K0
- D608 pad 1: /K0 -> /LED Group 2/Led Module 1/K0
- D609 pad 1: /K0 -> /LED Group 2/Led Module 1/K0
- D61 pad 1: /K2 -> /LED Group 0/Led Module 1/K2
- D610 pad 1: /K1 -> /LED Group 2/Led Module 1/K1
- D611 pad 1: /K1 -> /LED Group 2/Led Module 1/K1
- D612 pad 1: /K1 -> /LED Group 2/Led Module 1/K1
- D613 pad 1: /K1 -> /LED Group 2/Led Module 1/K1
- D614 pad 1: /K1 -> /LED Group 2/Led Module 1/K1
- D615 pad 1: /K1 -> /LED Group 2/Led Module 1/K1
- D616 pad 1: /K1 -> /LED Group 2/Led Module 1/K1
- D617 pad 1: /K1 -> /LED Group 2/Led Module 1/K1
- D618 pad 1: /K4 -> /LED Group 2/Led Module 1/K4
- D619 pad 1: /K4 -> /LED Group 2/Led Module 1/K4
- D62 pad 1: /K2 -> /LED Group 0/Led Module 1/K2
- D620 pad 1: /K4 -> /LED Group 2/Led Module 1/K4
- D621 pad 1: /K4 -> /LED Group 2/Led Module 1/K4
- D622 pad 1: /K4 -> /LED Group 2/Led Module 1/K4
- D623 pad 1: /K4 -> /LED Group 2/Led Module 1/K4
- D624 pad 1: /K4 -> /LED Group 2/Led Module 1/K4
- D625 pad 1: /K4 -> /LED Group 2/Led Module 1/K4
- D626 pad 1: /K3 -> /LED Group 2/Led Module 1/K3
- D627 pad 1: /K3 -> /LED Group 2/Led Module 1/K3
- D628 pad 1: /K3 -> /LED Group 2/Led Module 1/K3
- D629 pad 1: /K3 -> /LED Group 2/Led Module 1/K3
- D63 pad 1: /K2 -> /LED Group 0/Led Module 1/K2
- D630 pad 1: /K3 -> /LED Group 2/Led Module 1/K3
- D631 pad 1: /K3 -> /LED Group 2/Led Module 1/K3
- D632 pad 1: /K3 -> /LED Group 2/Led Module 1/K3
- D633 pad 1: /K3 -> /LED Group 2/Led Module 1/K3
- D634 pad 1: /K2 -> /LED Group 2/Led Module 1/K2
- D635 pad 1: /K2 -> /LED Group 2/Led Module 1/K2
- D636 pad 1: /K2 -> /LED Group 2/Led Module 1/K2
- D637 pad 1: /K2 -> /LED Group 2/Led Module 1/K2
- D638 pad 1: /K2 -> /LED Group 2/Led Module 1/K2
- D639 pad 1: /K2 -> /LED Group 2/Led Module 1/K2
- D64 pad 1: /K2 -> /LED Group 0/Led Module 1/K2
- D640 pad 1: /K2 -> /LED Group 2/Led Module 1/K2
- D641 pad 1: /K2 -> /LED Group 2/Led Module 1/K2
- D642 pad 1: /K5 -> /LED Group 2/Led Module 1/K5
- D643 pad 1: /K5 -> /LED Group 2/Led Module 1/K5
- D644 pad 1: /K5 -> /LED Group 2/Led Module 1/K5
- D645 pad 1: /K5 -> /LED Group 2/Led Module 1/K5
- D646 pad 1: /K5 -> /LED Group 2/Led Module 1/K5
- D647 pad 1: /K5 -> /LED Group 2/Led Module 1/K5
- D648 pad 1: /K5 -> /LED Group 2/Led Module 1/K5
- D649 pad 1: /K5 -> /LED Group 2/Led Module 1/K5
- D65 pad 1: /K2 -> /LED Group 0/Led Module 1/K2
- D650 pad 1: /K7 -> /LED Group 2/Led Module 1/K7
- D651 pad 1: /K7 -> /LED Group 2/Led Module 1/K7
- D652 pad 1: /K7 -> /LED Group 2/Led Module 1/K7
- D653 pad 1: /K7 -> /LED Group 2/Led Module 1/K7
- D654 pad 1: /K7 -> /LED Group 2/Led Module 1/K7
- D655 pad 1: /K7 -> /LED Group 2/Led Module 1/K7
- D656 pad 1: /K7 -> /LED Group 2/Led Module 1/K7
- D657 pad 1: /K7 -> /LED Group 2/Led Module 1/K7
- D658 pad 1: /K6 -> /LED Group 2/Led Module 1/K6
- D659 pad 1: /K6 -> /LED Group 2/Led Module 1/K6
- D66 pad 1: /K5 -> /LED Group 0/Led Module 1/K5
- D660 pad 1: /K6 -> /LED Group 2/Led Module 1/K6
- D661 pad 1: /K6 -> /LED Group 2/Led Module 1/K6
- D662 pad 1: /K6 -> /LED Group 2/Led Module 1/K6
- D663 pad 1: /K6 -> /LED Group 2/Led Module 1/K6
- D664 pad 1: /K6 -> /LED Group 2/Led Module 1/K6
- D665 pad 1: /K6 -> /LED Group 2/Led Module 1/K6
- D666 pad 1: /K0 -> /LED Group 2/Led Module 1/K0
- D667 pad 1: /K0 -> /LED Group 2/Led Module 1/K0
- D668 pad 1: /K0 -> /LED Group 2/Led Module 1/K0
- D669 pad 1: /K0 -> /LED Group 2/Led Module 1/K0
- D67 pad 1: /K5 -> /LED Group 0/Led Module 1/K5
- D670 pad 1: /K0 -> /LED Group 2/Led Module 1/K0
- D671 pad 1: /K0 -> /LED Group 2/Led Module 1/K0
- D672 pad 1: /K0 -> /LED Group 2/Led Module 1/K0
- D673 pad 1: /K0 -> /LED Group 2/Led Module 1/K0
- D674 pad 1: /K1 -> /LED Group 2/Led Module 1/K1
- D675 pad 1: /K1 -> /LED Group 2/Led Module 1/K1
- D676 pad 1: /K1 -> /LED Group 2/Led Module 1/K1
- D677 pad 1: /K1 -> /LED Group 2/Led Module 1/K1
- D678 pad 1: /K1 -> /LED Group 2/Led Module 1/K1
- D679 pad 1: /K1 -> /LED Group 2/Led Module 1/K1
- D68 pad 1: /K5 -> /LED Group 0/Led Module 1/K5
- D680 pad 1: /K1 -> /LED Group 2/Led Module 1/K1
- D681 pad 1: /K1 -> /LED Group 2/Led Module 1/K1
- D682 pad 1: /K4 -> /LED Group 2/Led Module 1/K4
- D683 pad 1: /K4 -> /LED Group 2/Led Module 1/K4
- D684 pad 1: /K4 -> /LED Group 2/Led Module 1/K4
- D685 pad 1: /K4 -> /LED Group 2/Led Module 1/K4
- D686 pad 1: /K4 -> /LED Group 2/Led Module 1/K4
- D687 pad 1: /K4 -> /LED Group 2/Led Module 1/K4
- D688 pad 1: /K4 -> /LED Group 2/Led Module 1/K4
- D689 pad 1: /K4 -> /LED Group 2/Led Module 1/K4
- D69 pad 1: /K5 -> /LED Group 0/Led Module 1/K5
- D690 pad 1: /K3 -> /LED Group 2/Led Module 1/K3
- D691 pad 1: /K3 -> /LED Group 2/Led Module 1/K3
- D692 pad 1: /K3 -> /LED Group 2/Led Module 1/K3
- D693 pad 1: /K3 -> /LED Group 2/Led Module 1/K3
- D694 pad 1: /K3 -> /LED Group 2/Led Module 1/K3
- D695 pad 1: /K3 -> /LED Group 2/Led Module 1/K3
- D696 pad 1: /K3 -> /LED Group 2/Led Module 1/K3
- D697 pad 1: /K3 -> /LED Group 2/Led Module 1/K3
- D698 pad 1: /K2 -> /LED Group 2/Led Module 1/K2
- D699 pad 1: /K2 -> /LED Group 2/Led Module 1/K2
- D7 pad 1: /K5 -> /LED Group 0/Led Module 1/K5
- D70 pad 1: /K5 -> /LED Group 0/Led Module 1/K5
- D700 pad 1: /K2 -> /LED Group 2/Led Module 1/K2
- D701 pad 1: /K2 -> /LED Group 2/Led Module 1/K2
- D702 pad 1: /K2 -> /LED Group 2/Led Module 1/K2
- D703 pad 1: /K2 -> /LED Group 2/Led Module 1/K2
- D704 pad 1: /K2 -> /LED Group 2/Led Module 1/K2
- D705 pad 1: /K2 -> /LED Group 2/Led Module 1/K2
- D706 pad 1: /K5 -> /LED Group 2/Led Module 1/K5
- D707 pad 1: /K5 -> /LED Group 2/Led Module 1/K5
- D708 pad 1: /K5 -> /LED Group 2/Led Module 1/K5
- D709 pad 1: /K5 -> /LED Group 2/Led Module 1/K5
- D71 pad 1: /K5 -> /LED Group 0/Led Module 1/K5
- D710 pad 1: /K5 -> /LED Group 2/Led Module 1/K5
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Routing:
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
